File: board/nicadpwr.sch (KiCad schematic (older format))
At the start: 31 parts, among them P1 CONN_SENSE, P2 CONN_CHARGE, P3 CONN_BAT, P4 CONN_VOUT, Q1 2N7000, Q2 BC547, Q3 TPCA8052H, U1 LM317T, U2 LM1117-5.0, U3 MC34063A

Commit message: Redesign of the board with fixes...
1. The charging voltage is now 5V (suitable for charging from USB)
   The charging now is connected directly to boost converter and
   linear out and battery charger are connected to the boost output.
   The converter raises battery or charging voltage to 6.3 volt.
2. Fixed problem with n-channel FET switch by using p-channel high
   side FET.
3. The board is enlarged and made single copper layer.
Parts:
- removed Q1: 2N7000, nicadpwr:2N7000-TO92, symbol Q_NMOS_DGS
- removed Q3: TPCA8052H, nicadpwr:TPCA8052H, symbol Q_NMOS_DGS
- added D6: RS1M, Diodes_SMD:D_SMA_Handsoldering, symbol D
- added Q1, Q3: Si4562DY, Housings_SOIC:SOIC-8_3.9x4.9mm_Pitch1.27mm, symbol Si4562DY
- added R10: 47K, Resistors_SMD:R_0805_HandSoldering, symbol R
- added R11: 100K, Resistors_SMD:R_0805_HandSoldering, symbol R
- added R9: 100, Resistors_SMD:R_0805_HandSoldering, symbol R
- C1: value 470uF -> 100uF; footprint Capacitors_ThroughHole:CP_Radial_D10.0mm_P5.00mm -> Capacitors_Tantalum_SMD:CP_Tantalum_Case-U_EIA-6032-15_Hand
- D1: value 1N3600 -> RS1M; footprint Diodes_ThroughHole:D_5W_P10.16mm_Horizontal -> Diodes_SMD:D_SMA_Handsoldering
- D2, D3: value 1N4148 -> RS1M
- D4: value 1N3600 -> 1N5819
- R1: value 100K -> 100
- R2: value 330K -> 47K
- R3: value 330K -> 100K
- R5: value 9.2K -> 100K
- R6: value 2.2K -> 27K
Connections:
- net labels added: CHARGE_IN
- wire segments 80 -> 109
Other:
- moved on the sheet: C1, C2, C3, C5, C6, R1, R2, R5, U2

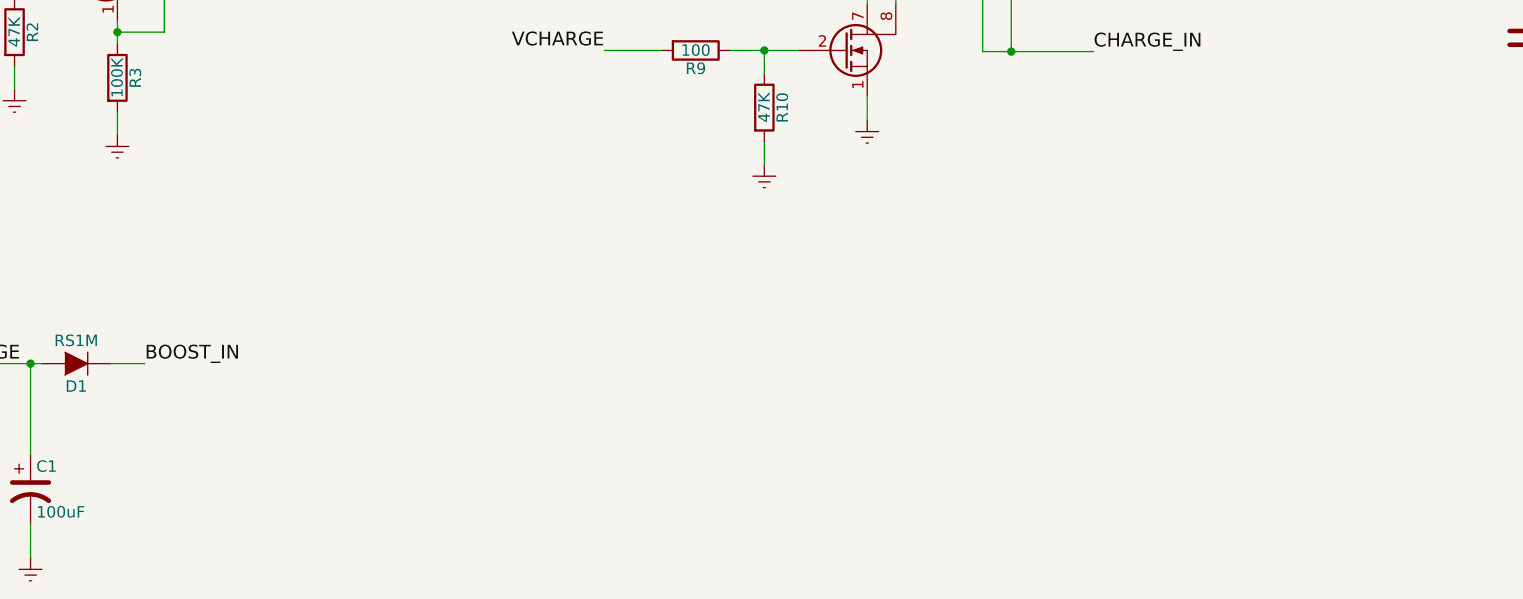
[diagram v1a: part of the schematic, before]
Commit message: Place todos on schematics before v3
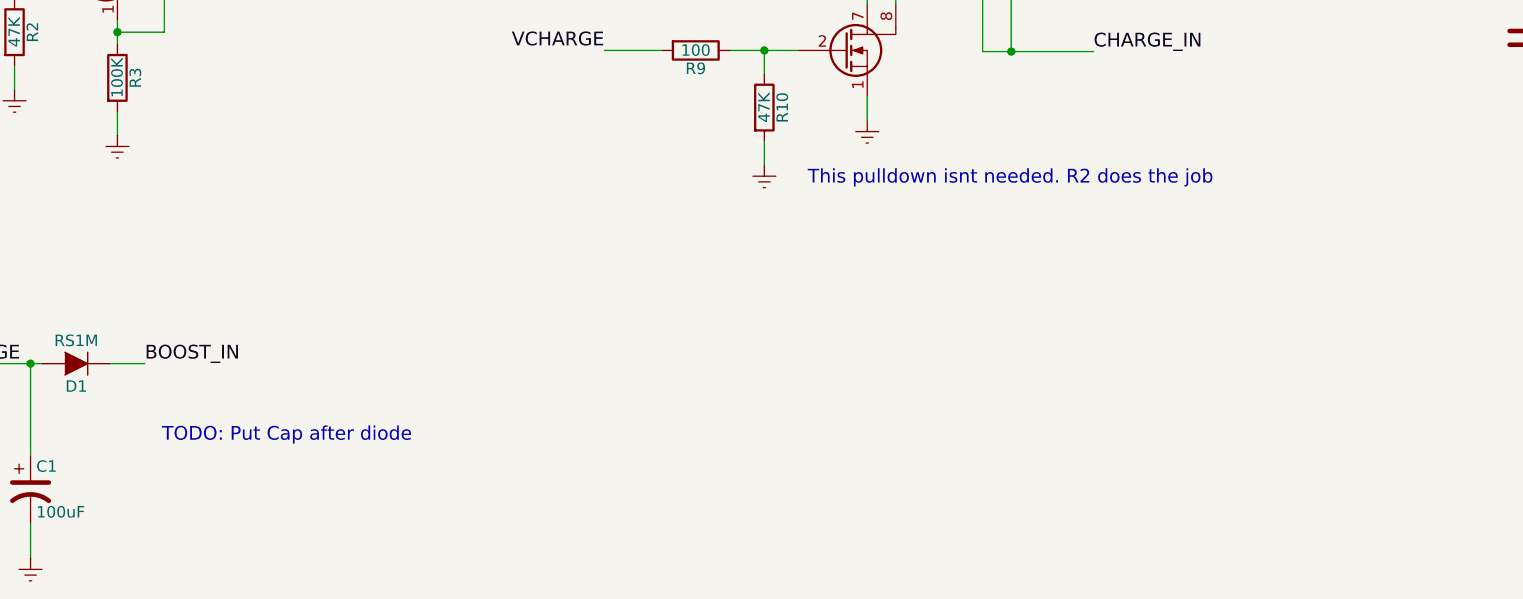
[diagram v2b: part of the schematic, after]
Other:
- note added: "TODO: Put Cap after diode"
- note added: "This pulldown isnt needed. R2 does the job"
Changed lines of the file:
@@
 	9665 1760 9665 1575
 Connection ~ 9665 1575
+Text Notes 2450 6475 0    60   ~ 0
+TODO: Put Cap after diode
+Text Notes 5275 5350 0    60   ~ 0
+This pulldown isnt needed. R2 does the job
 $EndSCHEMATC
